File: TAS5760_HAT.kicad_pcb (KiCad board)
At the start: 4 copper layers, 65 x 56 mm, 18 parts, among them J3 40HAT, J6 CONN_02X02, J9 CONN_01X02, Q1 DMG2305UX, Q2 DMMT5401, U2 CAT24C32

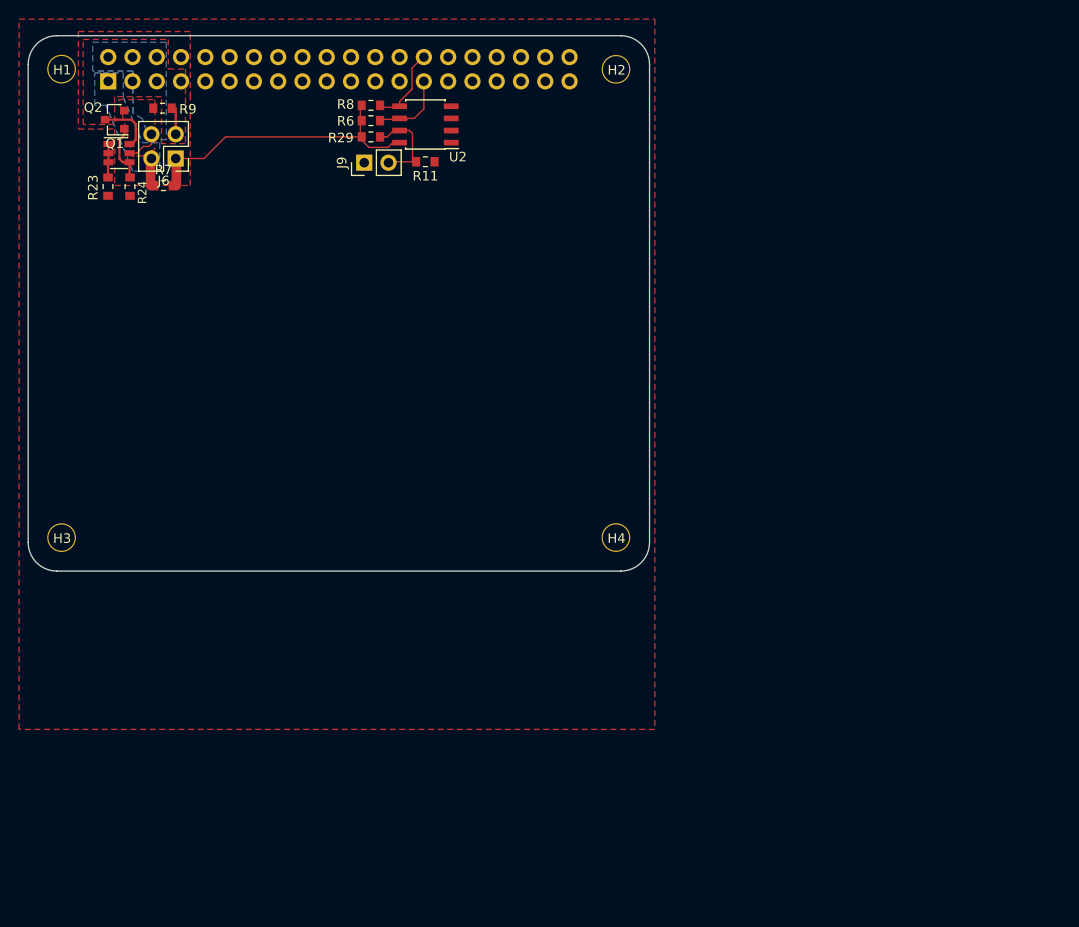
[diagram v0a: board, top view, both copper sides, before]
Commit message: 4 flip flops
Design with four flip flops and pll1708
Audio output jumper before filter
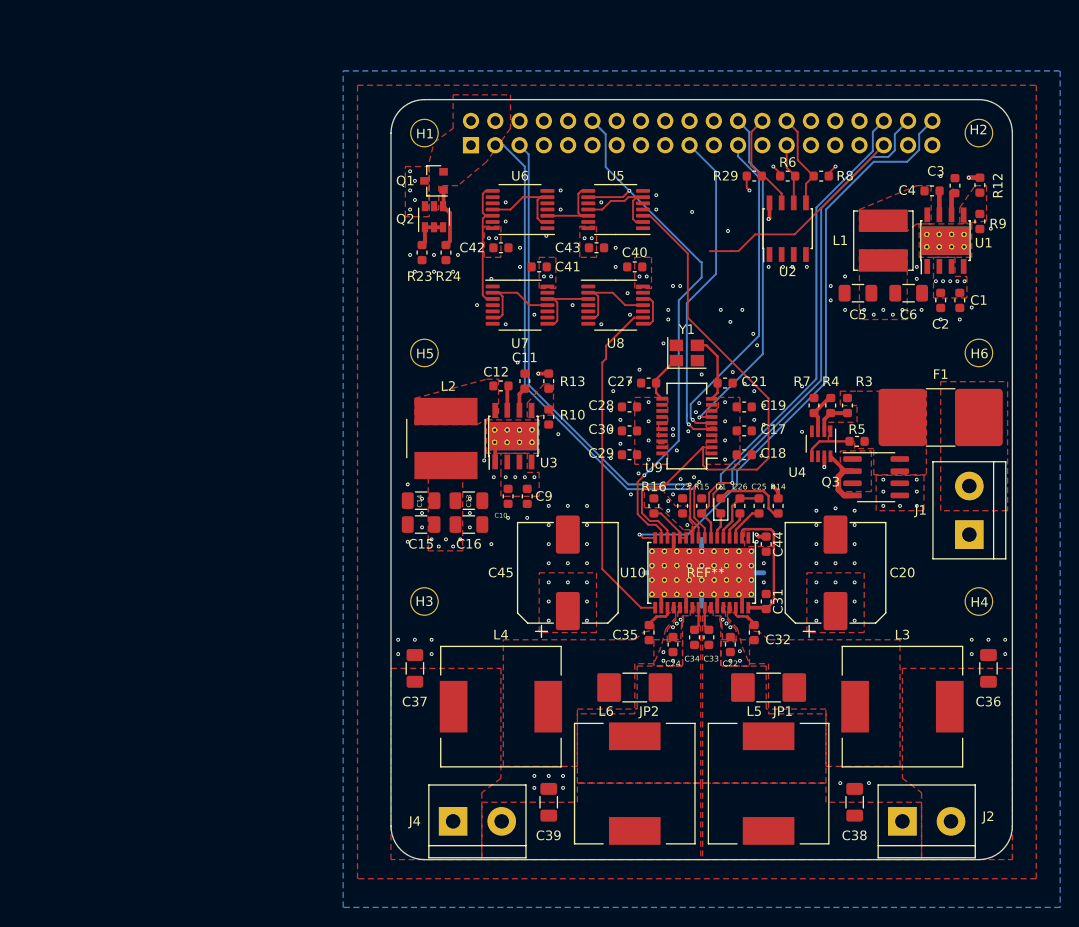
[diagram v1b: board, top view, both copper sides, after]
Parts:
- removed J6: CONN_02X02, Connector_PinHeader_2.54mm:PinHeader_2x02_P2.54mm_Vertical
- removed J9: CONN_01X02, Connector_PinHeader_2.54mm:PinHeader_1x02_P2.54mm_Vertical
- removed R11: DNP, Resistor_SMD:R_0603_1608Metric_Pad0.84x1.00mm_HandSolder
- added C1: 10u, Capacitor_SMD:C_0603_1608Metric, F.Cu at (176.0, 88.5)
- added C10: 220n, Capacitor_SMD:C_0603_1608Metric, F.Cu at (128.8, 109.0)
- added C11: 1u, Capacitor_SMD:C_0603_1608Metric, F.Cu at (130.5, 97.0)
- added C12: 0u1, Capacitor_SMD:C_0603_1608Metric, F.Cu at (128.0, 97.5)
- added C13: 22u, Capacitor_SMD:C_1206_3216Metric, F.Cu at (124.7, 109.5)
- added C14: 22u, Capacitor_SMD:C_1206_3216Metric, F.Cu at (119.7, 109.5)
- added C15: 22u, Capacitor_SMD:C_1206_3216Metric, F.Cu at (119.7, 112.0)
- added C16: 22u, Capacitor_SMD:C_1206_3216Metric, F.Cu at (124.7, 112.0)
- added C17: 10u, Capacitor_SMD:C_0603_1608Metric, F.Cu at (153.4, 102.2)
- added C18: 0u1, Capacitor_SMD:C_0603_1608Metric, F.Cu at (153.4, 104.7)
- added C19: 0u1, Capacitor_SMD:C_0603_1608Metric, F.Cu at (153.4, 99.7)
- added C2: 220n, Capacitor_SMD:C_0603_1608Metric, F.Cu at (174.0, 88.5)
- added C20: 470u, Capacitor_SMD:CP_Elec_10x10, F.Cu at (163.0, 117.0)
- added C21: 10p, Capacitor_SMD:C_0603_1608Metric, F.Cu at (151.4, 97.2)
- added C22: 0u1, Capacitor_SMD:C_0603_1608Metric, F.Cu at (152.0, 124.5)
- added C23: 1u, Capacitor_SMD:C_0603_1608Metric, F.Cu at (147.0, 110.0)
- added C24: 0u1, Capacitor_SMD:C_0603_1608Metric, F.Cu at (146.0, 124.5)
- added C25: 1u, Capacitor_SMD:C_0603_1608Metric, F.Cu at (155.0, 110.0)
- added C26: 1u, Capacitor_SMD:C_0603_1608Metric, F.Cu at (153.0, 110.0)
- added C27: 10p, Capacitor_SMD:C_0603_1608Metric, F.Cu at (143.4, 97.2)
- added C28: 0u1, Capacitor_SMD:C_0603_1608Metric, F.Cu at (141.4, 99.7)
- added C29: 0u1, Capacitor_SMD:C_0603_1608Metric, F.Cu at (141.4, 104.7)
- added C3: 1u, Capacitor_SMD:C_0603_1608Metric, F.Cu at (175.5, 76.5)
- added C30: 10u, Capacitor_SMD:C_0603_1608Metric, F.Cu at (141.4, 102.2)
- added C31: 1u, Capacitor_SMD:C_0603_1608Metric, F.Cu at (155.8, 120.0)
- added C32: 0u22, Capacitor_SMD:C_0603_1608Metric, F.Cu at (154.5, 123.2)
- added C33: 0u22, Capacitor_SMD:C_0603_1608Metric, F.Cu at (149.8, 123.8)
- added C34: 0u22, Capacitor_SMD:C_0603_1608Metric, F.Cu at (148.2, 123.8)
- added C35: 0u22, Capacitor_SMD:C_0603_1608Metric, F.Cu at (143.5, 123.2)
- added C36: 0u22, Capacitor_SMD:C_1206_3216Metric, F.Cu at (179.0, 127.0)
- added C37: 0u22, Capacitor_SMD:C_1206_3216Metric, F.Cu at (119.0, 127.0)
- added C38: 0u22, Capacitor_SMD:C_1206_3216Metric, F.Cu at (165.0, 141.0)
- added C39: 0u22, Capacitor_SMD:C_1206_3216Metric, F.Cu at (133.0, 141.0)
- added C4: 0u1, Capacitor_SMD:C_0603_1608Metric, F.Cu at (173.1, 77.0)
- added C40: 0u1, Capacitor_SMD:C_0603_1608Metric, F.Cu at (142.0, 85.0)
- added C41: 0u1, Capacitor_SMD:C_0603_1608Metric, F.Cu at (132.0, 85.0)
- added C42: 0u1, Capacitor_SMD:C_0603_1608Metric, F.Cu at (128.0, 83.0)
- added C43: 0u1, Capacitor_SMD:C_0603_1608Metric, F.Cu at (138.0, 83.0)
- added C44: 0u1, Capacitor_SMD:C_0603_1608Metric, F.Cu at (155.8, 114.0)
- added C45: 470u, Capacitor_SMD:CP_Elec_10x10, F.Cu at (135.0, 117.0)
- added C5: 22u, Capacitor_SMD:C_1206_3216Metric, F.Cu at (165.3, 87.8)
- added C6: 22u, Capacitor_SMD:C_1206_3216Metric, F.Cu at (170.7, 87.8)
- added C9: 10u, Capacitor_SMD:C_0603_1608Metric, F.Cu at (130.8, 109.0)
- added D1: LED, LED_SMD:LED_0603_1608Metric, F.Cu at (151.0, 110.0)
- added F1: Fuse, project_footprints:FuseHolder_OM_Schurter_OMH_125, F.Cu at (174.0, 100.8)
- added H5: 3mm_Mounting_Hole, project_footprints:NPTH_3mm_ID, F.Cu at (120.0, 94.0)
- added H6: 3mm_Mounting_Hole, project_footprints:NPTH_3mm_ID, F.Cu at (178.0, 94.0)
- added J1: SPK_A, TerminalBlock:TerminalBlock_bornier-2_P5.08mm, F.Cu at (177.0, 113.0)
- added J2: SPK_A, TerminalBlock:TerminalBlock_bornier-2_P5.08mm, F.Cu at (170.0, 143.0)
- added J4: SPK_A, TerminalBlock:TerminalBlock_bornier-2_P5.08mm, F.Cu at (123.0, 143.0)
- added JP1: Jumper_2_Open, project_footprints:Keystone_Jumper_5102, F.Cu at (156.0, 129.0)
- added JP2: Jumper_2_Open, project_footprints:Keystone_Jumper_5102, F.Cu at (142.0, 129.0)
- added L1: 10u, Inductor_SMD:L_Bourns_SRN6045TA, F.Cu at (168.0, 82.2)
- added L2: 8u, Inductor_SMD:L_Bourns_SRN8040TA, F.Cu at (122.2, 103.0)
- added L3: L, Inductor_SMD:L_12x12mm_H8mm, F.Cu at (170.0, 131.0)
- added L4: L, Inductor_SMD:L_12x12mm_H8mm, F.Cu at (128.0, 131.0)
- added L5: L, Inductor_SMD:L_12x12mm_H8mm, F.Cu at (156.0, 139.1)
- added L6: L, Inductor_SMD:L_12x12mm_H8mm, F.Cu at (142.0, 139.1)
- added Q3: FDS6890A, Package_SO:SOIC-8_3.9x4.9mm_P1.27mm, F.Cu at (167.2, 107.0)
- added R10: 24K9, Resistor_SMD:R_0603_1608Metric, F.Cu at (133.0, 100.7)
- added R12: 100K, Resistor_SMD:R_0603_1608Metric, F.Cu at (178.1, 76.5)
- added R13: 100K, Resistor_SMD:R_0603_1608Metric, F.Cu at (133.0, 97.0)
- added R14: 10K, Resistor_SMD:R_0603_1608Metric, F.Cu at (157.0, 110.0)
- added R15: 10K, Resistor_SMD:R_0603_1608Metric, F.Cu at (149.0, 110.0)
- added R16: 10K, Resistor_SMD:R_0603_1608Metric, F.Cu at (144.0, 110.0)
- added R3: 4M53, Resistor_SMD:R_0603_1608Metric, F.Cu at (164.2, 99.5)
- added R4: 215K, Resistor_SMD:R_0603_1608Metric, F.Cu at (162.5, 99.5)
- added R5: R, Resistor_SMD:R_0603_1608Metric, F.Cu at (165.2, 103.2)
- added U1: LMR33610ADDAR, Package_SO:Texas_HSOP-8-1EP_3.9x4.9mm_P1.27mm_ThermalVias, F.Cu at (174.5, 82.2)
- added U10: TAS5760, TAS5760_HAT:HTSSOP-32_backsolder, F.Cu at (149.0, 117.0)
- added U3: LMR33630ADDA, Package_SO:Texas_HSOP-8-1EP_3.9x4.9mm_P1.27mm_ThermalVias, F.Cu at (129.3, 102.7)
- added U4: LTC4365TS8, Package_TO_SOT_SMD:TSOT-23-8, F.Cu at (161.5, 103.5)
- added U5: 74HC74, Package_SO:TSSOP-14_4.4x5mm_P0.65mm, F.Cu at (140.0, 79.0)
- added U6: 74HC74, Package_SO:TSSOP-14_4.4x5mm_P0.65mm, F.Cu at (130.0, 79.0)
- added U7: 74HC74, Package_SO:TSSOP-14_4.4x5mm_P0.65mm, F.Cu at (130.0, 89.0)
- added U8: 74HC74, Package_SO:TSSOP-14_4.4x5mm_P0.65mm, F.Cu at (140.0, 89.0)
- added U9: PLL1708, Package_SO:SSOP-20_3.9x8.7mm_P0.635mm, F.Cu at (147.4, 101.7)
- added Y1: 27MHz, Crystal:Crystal_SMD_SeikoEpson_FA238-4Pin_3.2x2.5mm, F.Cu at (147.4, 94.0)
- R23, R24, R29: footprint Resistor_SMD:R_0603_1608Metric_Pad0.84x1.00mm_HandSolder -> Resistor_SMD:R_0603_1608Metric
- R6, R8: value 3.9K -> 3K9; footprint Resistor_SMD:R_0603_1608Metric_Pad0.84x1.00mm_HandSolder -> Resistor_SMD:R_0603_1608Metric
- R7: value DNP -> 86K6; footprint Resistor_SMD:R_0603_1608Metric_Pad0.84x1.00mm_HandSolder -> Resistor_SMD:R_0603_1608Metric
- R9: value DNP -> 43K2; footprint Resistor_SMD:R_0603_1608Metric_Pad0.84x1.00mm_HandSolder -> Resistor_SMD:R_0603_1608Metric
- moved R9 86.3 mm to (178.1, 80.2), turned to 270 degrees
- moved R7 71.8 mm to (160.8, 99.5), turned to 90 degrees
- moved R8 47.7 mm to (161.5, 75.5), turned to 180 degrees
- moved R6 44.0 mm to (158.0, 75.5)
- moved R29 40.3 mm to (154.5, 75.5)
- moved U2 39.4 mm to (158.0, 81.0), turned to 90 degrees
- moved H4 38.6 mm to (178.0, 120.0)
- moved H1 38.5 mm to (120.0, 71.0)
- moved H3 38.5 mm to (120.0, 120.0)
- moved H2 38.5 mm to (178.0, 71.0)
- moved J3 38.5 mm to (124.9, 72.3)
- moved Q1 34.0 mm to (121.0, 76.0)
- moved R24 33.8 mm to (122.2, 83.5)
- moved Q2 33.6 mm to (121.0, 79.8), turned to 90 degrees
- moved R23 33.6 mm to (119.8, 83.5)
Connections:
- net Net-(J3-Pad17) renamed /CLK_DIS
- J3 pad 1: /P3V3_HAT -> Net-(J3-Pad1)
- J3 pad 12: Net-(J3-Pad12) -> /BITCLK
- J3 pad 19: Net-(J3-Pad19) -> /MOSI
- J3 pad 23: Net-(J3-Pad23) -> /SPI_CLK
- J3 pad 24: Net-(J3-Pad24) -> /SS
- J3 pad 26: Net-(J3-Pad26) -> /WP
- J3 pad 3: Net-(J3-Pad3) -> /SDA
- J3 pad 35: Net-(J3-Pad35) -> /LRCLK
- J3 pad 36: Net-(J3-Pad36) -> /~SPK_FAULT
- J3 pad 38: Net-(J3-Pad38) -> /~SPK_SD
- J3 pad 40: Net-(J3-Pad40) -> /DATA_OUT
- J3 pad 5: Net-(J3-Pad5) -> /SCL
- R29 pad 2: Net-(J9-Pad2) -> /WP
- R7 pad 1: /P3V3_HAT -> Net-(R4-Pad2)
- R7 pad 2: /P3V3 -> GND
- R9 pad 1: /P5V_HAT -> Net-(R12-Pad2)
- R9 pad 2: /P5V -> GND
- U2 pad 7: Net-(J9-Pad2) -> /WP
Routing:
- net /DATA_OUT: track 0.00 -> 62.7 mm, vias 0 -> 1
- net /LRCLK: track 0.00 -> 58.6 mm
- net /BITCLK: track 0.00 -> 57.2 mm, vias 0 -> 2
- net /SDA: track 0.00 -> 56.6 mm, vias 0 -> 1
- net /MCLK: track 0.00 -> 56.3 mm
- net /~SPK_SD: track 0.00 -> 54.8 mm, vias 0 -> 1
- net /SCL: track 0.00 -> 52.6 mm, vias 0 -> 1
- net /~SPK_FAULT: track 0.00 -> 51.6 mm, vias 0 -> 1
- net GND: track 0.00 -> 38.7 mm, vias 0 -> 142
- net /SS: track 0.00 -> 36.2 mm, vias 0 -> 1
- net /SPI_CLK: track 0.00 -> 34.8 mm, vias 0 -> 1
- net /MOSI: track 0.00 -> 34.5 mm, vias 0 -> 1
- net /P3V3: track 31.3 -> 9.73 mm, vias 0 -> 22
- net Net-(C31-Pad1): track 0.00 -> 14.6 mm
- net Net-(U6-Pad12): track 0.00 -> 14.0 mm
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- added copper zone on F.Cu, net /P3V3
- added copper zone on In2.Cu, net /P3V3
- added copper zone on In2.Cu, net /P5V
- added copper zone on B.Cu, net GND
- added copper zone on In1.Cu, net GND
- added copper zone on F.Cu, net Net-(C12-Pad2)
- added copper zone on F.Cu, net Net-(C32-Pad2)
- added copper zone on F.Cu, net Net-(C33-Pad2)
- added copper zone on F.Cu, net Net-(C34-Pad2)
- added copper zone on F.Cu, net Net-(C35-Pad2)
- added copper zone on F.Cu, net Net-(C36-Pad2)
- added copper zone on F.Cu, net Net-(C37-Pad1)
- added copper zone on F.Cu, net Net-(C38-Pad1)
- added copper zone on F.Cu, net Net-(C39-Pad2)
- added copper zone on F.Cu, net Net-(C4-Pad2)
- added copper zone on F.Cu, net Net-(F1-Pad1)
- added copper zone on F.Cu, net Net-(F1-Pad2)
- added copper zone on F.Cu, net Net-(Q3-Pad1)
- added copper zone on F.Cu, net Net-(R10-Pad1)
- added copper zone on F.Cu, net Net-(R12-Pad2)
- added copper zone on F.Cu, net VDD
- added copper zone on In2.Cu, net VDD
- removed copper zone on B.Cu, net /P3V3_HAT
- removed copper zone on B.Cu, net /P5V_HAT
- removed copper zone on In2.Cu, net GND
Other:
- board size 65 x 56 mm -> 65 x 79.5 mm
- board text removed: "If you want to use an SMT 40-pin header, please move the top edge up by 0.5mm and locate the header in the same location as the current TH part."
- board text removed: "This is a HAT compatible PCB starting design based on the official Raspberry Pi specs at: https://github.com/raspberrypi/hats/blob/master/designguide.md Currently the camera slot and display cutout are not here. See the schematic for the details on the EEPROM and power setup. This board does have the correct components for powering the Pi via the HAT. If you need the Pi to provide 5V or 3.3V, ple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"

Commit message: Updated clock circuit to WM8804
Added optional toslink input and output since wm8804 has digital
input and output. Removed old clock dividing circuit since not needed
since wm8804 has this for free
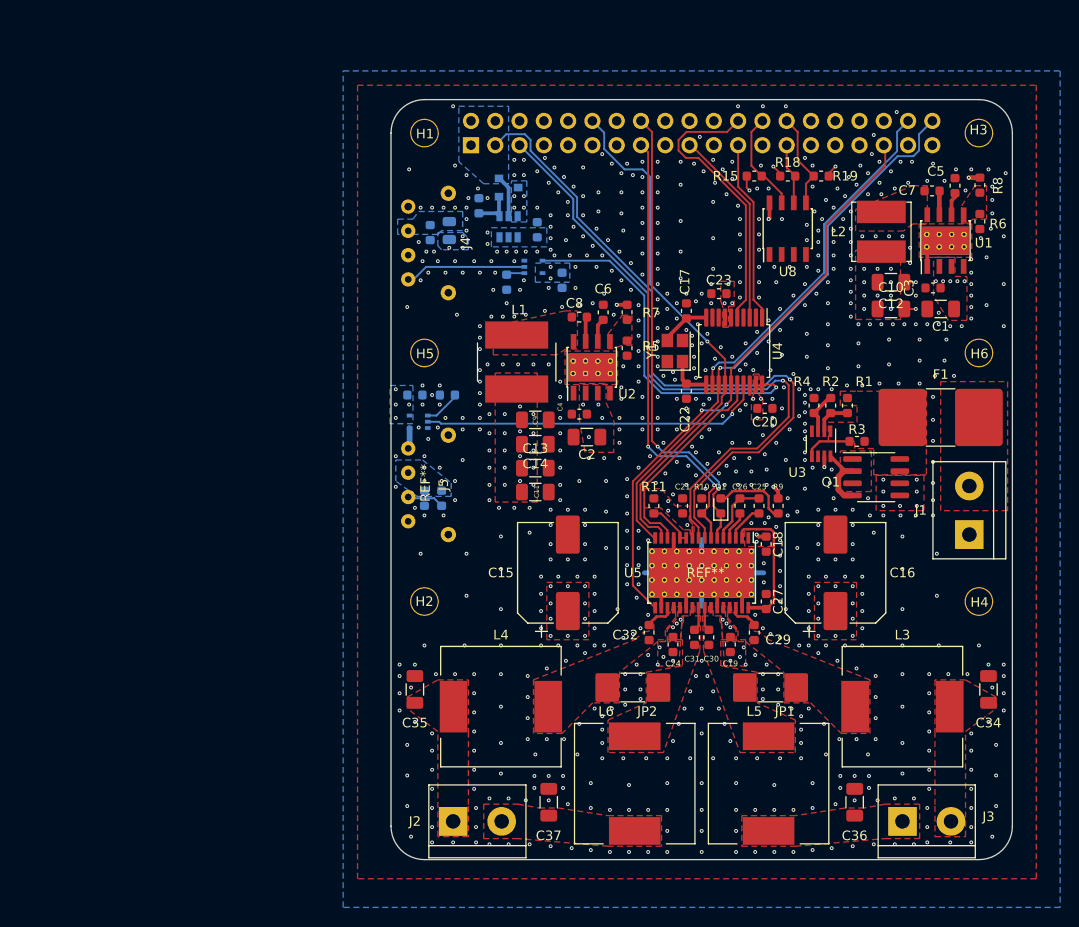
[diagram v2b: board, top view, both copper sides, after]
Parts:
- removed the C10 at (128.8, 109.0)
- removed the C12 at (128.0, 97.5)
- removed the C16 at (124.7, 112.0)
- removed the C18 at (153.4, 104.7)
- removed the C19 at (153.4, 99.7)
- removed the C21 at (151.4, 97.2)
- removed the C27 at (143.4, 97.2)
- removed the C29 at (141.4, 104.7)
- removed the C30 at (141.4, 102.2)
- removed the C37 at (119.0, 127.0)
- removed C40, C41, C42, C43: 0u1, Capacitor_SMD:C_0603_1608Metric
- removed C45: 470u, Capacitor_SMD:CP_Elec_10x10
- removed the Q1 at (121.0, 76.0)
- removed the R15 at (149.0, 110.0)
- removed R23, R24: 22, Resistor_SMD:R_0603_1608Metric
- removed the U3 at (129.3, 102.7)
- removed the U5 at (140.0, 79.0)
- removed the U8 at (140.0, 89.0)
- removed U9: PLL1708, Package_SO:SSOP-20_3.9x8.7mm_P0.635mm
- added C2: 10u, Capacitor_SMD:C_1206_3216Metric, F.Cu at (137.0, 102.8)
- added C20: 0u1, Capacitor_SMD:C_0603_1608Metric, F.Cu at (155.6, 99.8)
- added C22: 10p, Capacitor_SMD:C_0603_1608Metric, F.Cu at (147.4, 98.0)
- added C23: 0u1, Capacitor_SMD:C_0603_1608Metric, F.Cu at (150.8, 87.8)
- added C33: 0u1, Capacitor_SMD:C_0603_1608Metric, B.Cu at (119.0, 98.4)
- added C35: 0u22, Capacitor_SMD:C_1206_3216Metric, F.Cu at (119.0, 129.2)
- added C38: 0u1, Capacitor_SMD:C_0603_1608Metric, B.Cu at (120.6, 81.4)
- added C39: 0u1, Capacitor_SMD:C_0603_1608Metric, B.Cu at (120.0, 109.2)
- added C4: 220n, Capacitor_SMD:C_0603_1608Metric, F.Cu at (136.2, 100.4)
- added C6: 1u, Capacitor_SMD:C_0603_1608Metric, F.Cu at (138.7, 89.8)
- added C8: 0u1, Capacitor_SMD:C_0603_1608Metric, F.Cu at (136.2, 90.2)
- added J4: TORX1950, TAS5760_HAT:TORX1950, F.Cu at (122.5, 82.5)
- added J5: TOTX1950, TAS5760_HAT:TOTX1950, F.Cu at (122.5, 107.8)
- added L7: 47u, Inductor_SMD:L_0805_2012Metric, B.Cu at (122.6, 81.2)
- added Q3: DMG2305UX, Package_TO_SOT_SMD:SOT-23, B.Cu at (128.8, 76.7)
- added R12: 100K, Resistor_SMD:R_0603_1608Metric, B.Cu at (128.6, 86.6)
- added R14: 5K6, Resistor_SMD:R_0603_1608Metric, B.Cu at (121.8, 109.2)
- added R16: 10K, Resistor_SMD:R_0603_1608Metric, B.Cu at (131.8, 81.1)
- added R17: 47K, Resistor_SMD:R_0603_1608Metric, B.Cu at (125.7, 78.6)
- added R5: 24K9, Resistor_SMD:R_0603_1608Metric, F.Cu at (141.2, 93.5)
- added R7: 100K, Resistor_SMD:R_0603_1608Metric, F.Cu at (141.2, 89.8)
- added U2: LMR33630ADDA, Package_SO:Texas_HSOP-8-1EP_3.9x4.9mm_P1.27mm_ThermalVias, F.Cu at (137.5, 95.5)
- added U4: WM8804, TAS5760_HAT:SSOP-20_5.3x7.2mm_P0.65mm, F.Cu at (152.4, 93.8)
- C1: footprint Capacitor_SMD:C_0603_1608Metric -> Capacitor_SMD:C_1206_3216Metric
- C11: value 1u -> 22u; footprint Capacitor_SMD:C_0603_1608Metric -> Capacitor_SMD:C_1206_3216Metric
- C15: value 22u -> 470u; footprint Capacitor_SMD:C_1206_3216Metric -> Capacitor_SMD:CP_Elec_10x10
- C17: value 10u -> 10p
- C28, Q2, R13: moved to B.Cu
- C9: value 10u -> 22u; footprint Capacitor_SMD:C_0603_1608Metric -> Capacitor_SMD:C_1206_3216Metric
- L1: value 10u -> 8u; footprint Inductor_SMD:L_Bourns_SRN6045TA -> Inductor_SMD:L_Bourns_SRN8040TA
- L2: value 8u -> 10u; footprint Inductor_SMD:L_Bourns_SRN8040TA -> Inductor_SMD:L_Bourns_SRN6045TA
- R10: value 24K9 -> 10K
- R3: renamed from R5; value R -> 100K
- U6, U7: value 74HC74 -> 74AHC1G125; footprint Package_SO:TSSOP-14_4.4x5mm_P0.65mm -> TAS5760_HAT:TSSOP-5; moved to B.Cu
- moved L2 50.4 mm to (167.8, 81.3)
- moved L1 40.4 mm to (129.7, 95.0)
- moved R10 18.5 mm to (149.0, 110.0), turned to 90 degrees
- moved U7 16.2 mm to (119.4, 101.2), turned to 180 degrees
- moved C15 16.2 mm to (135.0, 117.0), turned to 90 degrees
- moved C28 15.0 mm to (134.4, 86.4), turned to 270 degrees
- moved C17 13.9 mm to (147.4, 89.6), turned to 90 degrees
- moved C14 13.3 mm to (131.6, 103.5), turned to 0 degrees
- moved C11 11.7 mm to (131.6, 108.5), turned to 0 degrees
- moved R13 10.7 mm to (122.4, 98.4), turned to 0 degrees
- moved C9 8.05 mm to (131.6, 101.0), turned to 0 degrees
- moved Q2 7.87 mm to (128.8, 80.8)
- moved C13 7.74 mm to (131.6, 106.0)
- moved U6 6.16 mm to (131.4, 85.0), turned to 0 degrees
- moved C10 3.82 mm to (168.8, 89.4), turned to 0 degrees
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- renumbered C5 to C10, C6 to C12, C20 to C16, C44 to C18, C22 to C19, C23 to C21, C31 to C27, C32 to C29, C2 to C3, C33 to C30, C34 to C31, C35 to C32, C36 to C34, C38 to C36, C39 to C37, C3 to C5, C4 to C7, H3 to H2, H2 to H3, J4 to J2, J2 to J3, J3 to J6, Q3 to Q1, R3 to R1, R16 to R11, R29 to R15, R6 to R18, R8 to R19, R4 to R2, R7 to R4, R9 to R6, R12 to R8, R14 to R9, U4 to U3, U10 to U5, U2 to U8
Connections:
- net /CLK_DIS renamed Net-(J6-Pad17)
- C11 pad 1: GND -> /P5V
- C11 pad 2: Net-(C11-Pad2) -> GND
- C15 pad 1: /P5V -> VDD
- C17 pad 1: /P3V3 -> Net-(C17-Pad1)
- C7 pad 2: Net-(C4-Pad2) -> Net-(C7-Pad2)
- C9 pad 1: VDD -> /P5V
- J6 pad 15: Net-(J3-Pad15) -> /~SPK_SD
- J6 pad 16: Net-(J3-Pad16) -> /~SPK_FAULT
- J6 pad 36: /~SPK_FAULT -> Net-(J6-Pad36)
- J6 pad 38: /~SPK_SD -> /DATA_IN
- L1 pad 1: Net-(C4-Pad2) -> Net-(C8-Pad2)
- L1 pad 2: /P3V3 -> /P5V
- L2 pad 1: Net-(C12-Pad2) -> Net-(C7-Pad2)
- L2 pad 2: /P5V -> /P3V3
- R10 pad 1: Net-(R10-Pad1) -> /~SPK_SD
- R13 pad 1: /P5V -> GND
- R13 pad 2: Net-(R10-Pad1) -> Net-(R13-Pad2)
- U1 pad 8: Net-(C4-Pad2) -> Net-(C7-Pad2)
- U6 pad 1: GND -> Net-(R12-Pad1)
- U6 pad 2: Net-(U6-Pad11) -> Net-(J4-Pad1)
- U6 pad 3: Net-(U5-Pad12) -> GND
- U6 pad 4: GND -> Net-(U4-Pad20)
- U6 pad 5: Net-(U6-Pad5) -> /P3V3
- U7 pad 1: GND -> Net-(R13-Pad2)
- U7 pad 2: Net-(U7-Pad11) -> Net-(U4-Pad17)
- U7 pad 3: Net-(U6-Pad12) -> GND
- U7 pad 4: GND -> Net-(J5-Pad4)
- U7 pad 5: Net-(U7-Pad5) -> /P5V
- Y1 pad 3: Net-(C21-Pad1) -> Net-(C17-Pad1)
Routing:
- net /DATA_IN: track 0.00 -> 37.0 mm, vias 0 -> 1
- net Net-(U4-Pad20): track 0.00 -> 37.0 mm, vias 0 -> 1
- net Net-(U4-Pad17): track 0.00 -> 35.9 mm, vias 0 -> 1
- net /MCLK: track 56.3 -> 23.0 mm
- net /SDA: track 56.6 -> 72.7 mm
- net /SPI_CLK: track 34.8 -> 19.2 mm, vias 1 -> 0
- net /SCL: track 52.6 -> 67.7 mm
- net Net-(U6-Pad12): track 14.0 -> 0.00 mm
- net /MOSI: track 34.5 -> 20.7 mm, vias 1 -> 0
- net Net-(J4-Pad1): track 0.00 -> 12.7 mm
- net Net-(U8-Pad11): track 10.5 -> 0.00 mm
- net Net-(U6-Pad11): track 10.5 -> 0.00 mm
- net Net-(U7-Pad11): track 10.5 -> 0.00 mm
- net Net-(U5-Pad11): track 10.5 -> 0.00 mm
- net Net-(U5-Pad12): track 8.60 -> 0.00 mm
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- added copper zone on F.Cu, net (none)
- added copper zone on B.Cu, net /P3V3
- added copper zone on B.Cu, net /P5V
- added copper zone on B.Cu, net /P5V_HAT
- added copper zone on B.Cu, net Net-(C17-Pad1)
- added copper zone on F.Cu, net Net-(C7-Pad2)
- added copper zone on F.Cu, net Net-(C8-Pad2)
- added copper zone on B.Cu, net Net-(Q2-Pad1)
- added copper zone on F.Cu, net Net-(R5-Pad1)
- removed copper zone on F.Cu, net /P5V_HAT
- removed copper zone on F.Cu, net Net-(C12-Pad2)
- removed copper zone on F.Cu, net Net-(C4-Pad2)
- removed copper zone on F.Cu, net Net-(R10-Pad1)
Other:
- net class Default: trace_width 0.15 -> 0.2
- rule pad_to_mask_clearance: 0.1 -> 0.05
- rule trace_min: 0.15 -> 0.2
